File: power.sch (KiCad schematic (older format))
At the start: 25 parts, among them U3 LD3985M18R, U4 LM22676QMRX-5.0, U5 LD3985M33R

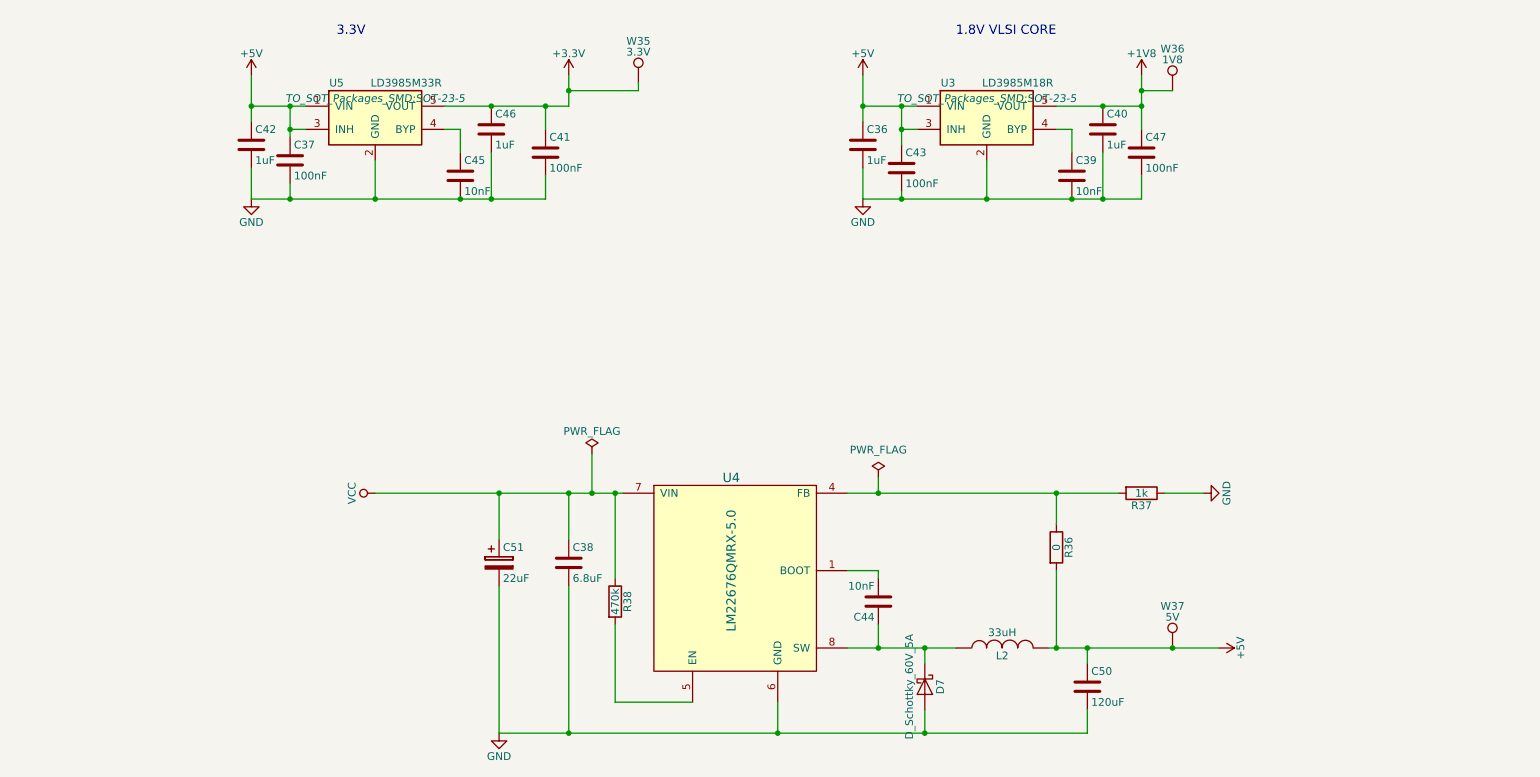
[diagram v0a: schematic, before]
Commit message: Changed butten connectors
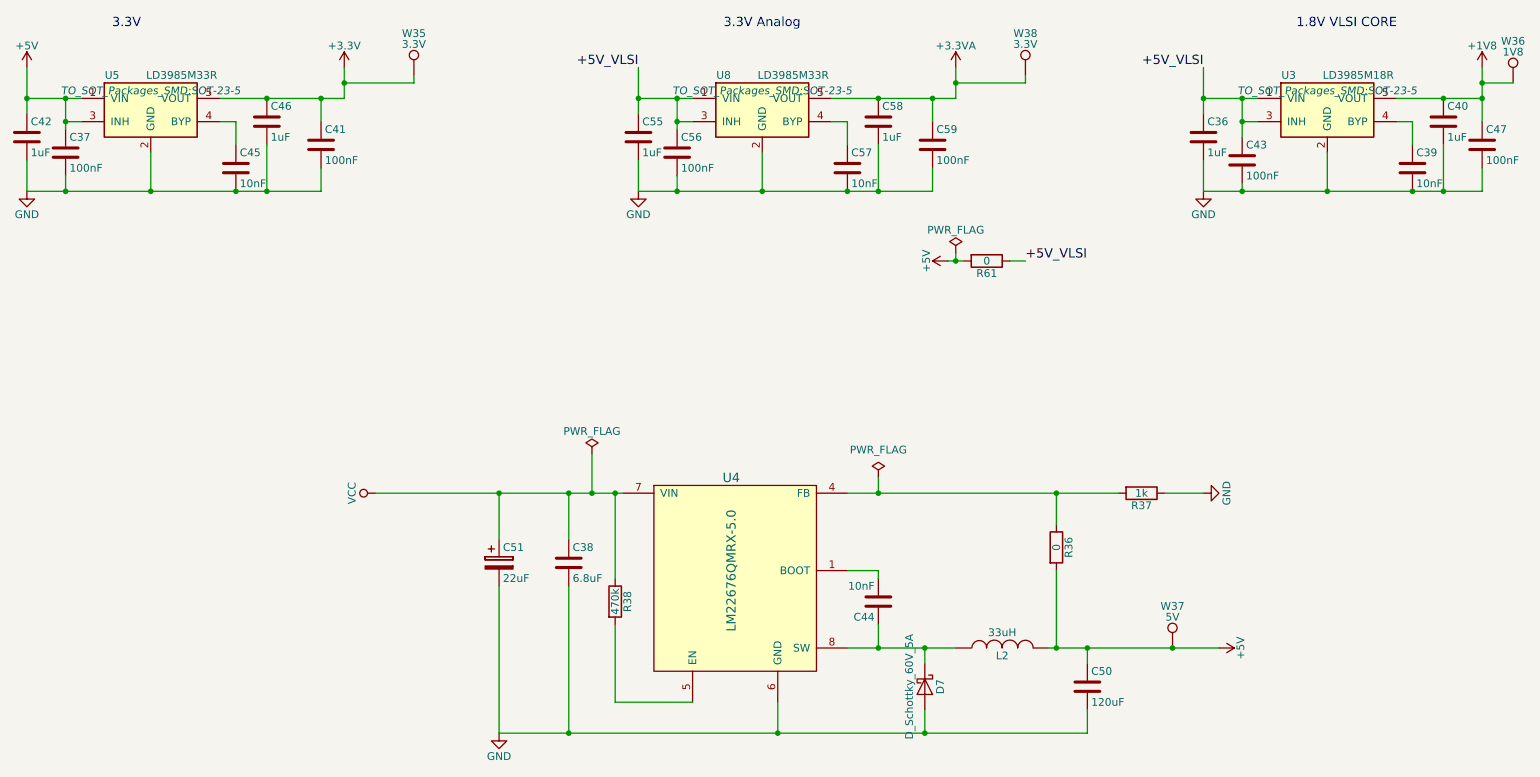
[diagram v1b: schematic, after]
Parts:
- added C55, C58: 1uF, Capacitors_SMD:C_0603, symbol C
- added C56, C59: 100nF, Capacitors_SMD:C_0402, symbol C
- added C57: 10nF, Capacitors_SMD:C_0603, symbol C
- added R61: 0, Resistors_SMD:R_0603, symbol R
- added U8: LD3985M33R, TO_SOT_Packages_SMD:SOT-23-5, symbol LD3985M33R
- added W38: 3.3V, Measurement_Points:Measurement_Point_Round-SMD-Pad_Small, symbol TEST_1P
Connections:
- net +5V: now also R61.2; no longer C36.1, C43.1, U3.1 (VIN), U3.3 (INH)
- net GND: now also C55.2, C56.2, C57.2, C58.2, C59.2, U8.2 (GND)
- new net: C57.1, U8.4 (BYP)
- new net +3.3VA: C58.1, C59.1, U8.5 (VOUT), W38.1
- new net +5V_VLSI: C36.1, C43.1, C55.1, C56.1, R61.1, U3.1 (VIN), U3.3 (INH), U8.1 (VIN), U8.3 (INH)
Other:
- note added: "3.3V Analog"
- moved on the sheet: C36, C37, C39, C40, C41, C42, C43, C45, C46, C47, U3, U5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
